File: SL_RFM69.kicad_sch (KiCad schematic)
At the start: 8 parts, among them SW1 SW_DIP_x08

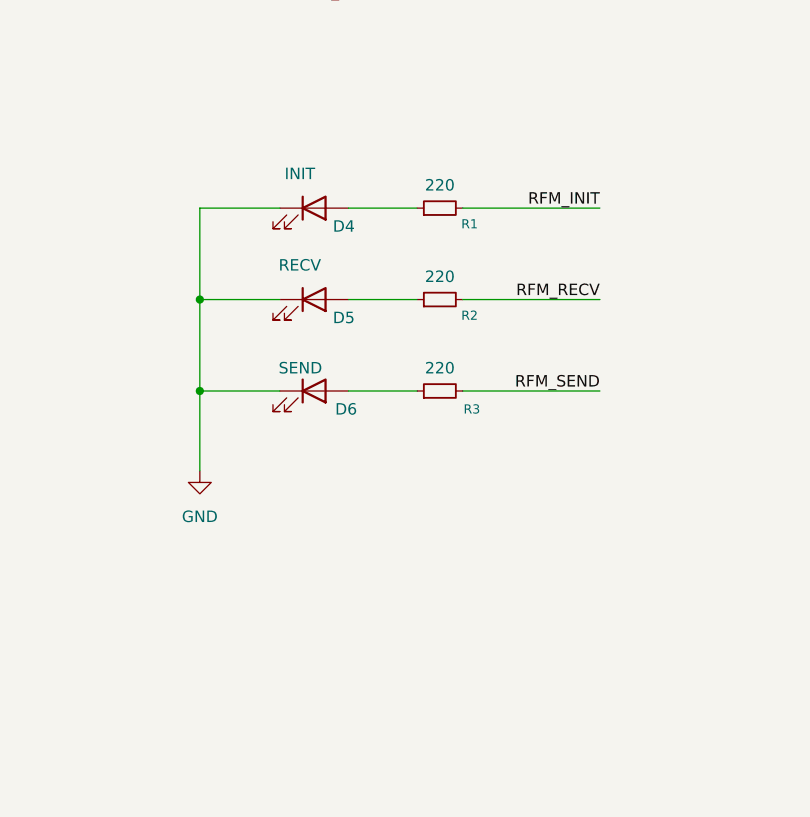
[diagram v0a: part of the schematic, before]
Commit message: Add power led
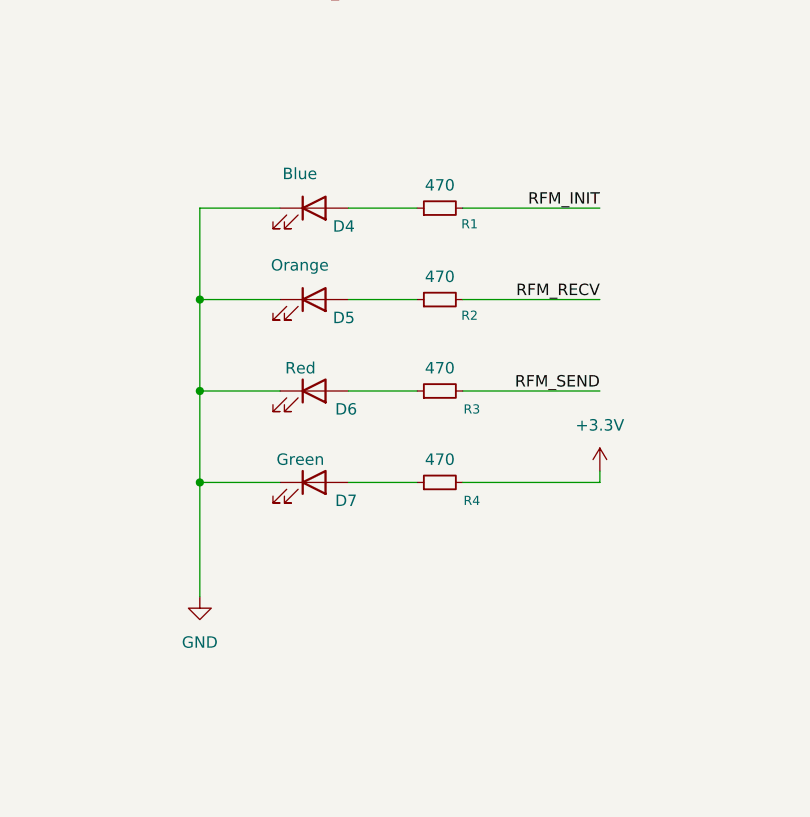
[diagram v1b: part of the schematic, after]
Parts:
- added D7: Green, LED_SMD:LED_0805_2012Metric, symbol Device:LED
- added R4: 470, LED_SMD:LED_0805_2012Metric, symbol Device:R_Small
- D4: value INIT -> Blue
- D5: value RECV -> Orange
- D6: value SEND -> Red
- R1, R2, R3: value 220 -> 470
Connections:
- net +3.3V: now also R4.2
- net GND: now also D7.1 (K)
- new net: D7.2 (A), R4.1

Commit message: Add partnumbers
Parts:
- D4: JLCPCB (none) -> C2293; LCSC (none) -> C2293
- D5: JLCPCB (none) -> C84262; LCSC (none) -> C84262
- D6: JLCPCB (none) -> C84256; LCSC (none) -> C84256
- D7: JLCPCB (none) -> C2297; LCSC (none) -> C2297
- R1, R2, R3, R4: JLCPCB (none) -> C17710; LCSC (none) -> C17710
- SW1: JLCPCB (none) -> C559170
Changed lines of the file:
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@@
+			)
+		)
+		(property "JLCPCB" "C84262"
+			(at 50.8 92.71 0)
+			(hide yes)
+			(show_name no)
+			(do_not_autoplace no)
+			(effects
+				(font
+					(size 1.27 1.27)
+				)
+			)
+		)
+		(property "LCSC" "C84262"
+			(at 50.8 92.71 0)
+			(hide yes)
+			(show_name no)
+			(do_not_autoplace no)
+			(effects
+				(font
+					(size 1.27 1.27)
+				)
 			)
 		)
@@
 		(property "Description" "Resistor, small symbol"
 			(at 64.77 113.03 0)
+			(hide yes)
+			(show_name no)
+			(do_not_autoplace no)
+			(effects
+				(font
+					(size 1.27 1.27)
+				)
+			)
+		)
+		(property "JLCPCB" "C17710"
+			(at 64.77 113.03 90)
+			(hide yes)
+			(show_name no)
+			(do_not_autoplace no)
+			(effects
+				(font
+					(size 1.27 1.27)
+				)
+			)
+		)
+		(property "LCSC" "C17710"
+			(at 64.77 113.03 90)
 			(hide yes)
 			(show_name no)
@@
 			)
 		)
+		(property "JLCPCB" "C2293"
+			(at 50.8 82.55 0)
+			(hide yes)
+			(show_name no)
+			(do_not_autoplace no)
+			(effects
+				(font
+					(size 1.27 1.27)
+				)
+			)
+		)
+		(property "LCSC" "C2293"
+			(at 50.8 82.55 0)
+			(hide yes)
+			(show_name no)
+			(do_not_autoplace no)
+			(effects
+				(font
+					(size 1.27 1.27)
+				)
+			)
+		)
 		(pin "2"
 		)
@@
 			)
 		)
+		(property "JLCPCB" "C84256"
+			(at 50.8 102.87 0)
+			(hide yes)
+			(show_name no)
+			(do_not_autoplace no)
+			(effects
+				(font
+					(size 1.27 1.27)
+				)
+			)
+		)
+		(property "LCSC" "C84256"
+			(at 50.8 102.87 0)
+			(hide yes)
+			(show_name no)
+			(do_not_autoplace no)
+			(effects
+				(font
+					(size 1.27 1.27)
+				)
+			)
+		)
 		(pin "2"
 		)
@@
 		(property "Description" "Resistor, small symbol"
 			(at 64.77 102.87 0)
+			(hide yes)
+			(show_name no)
+			(do_not_autoplace no)
+			(effects
+				(font
+					(size 1.27 1.27)
+				)
+			)
+		)
+		(property "JLCPCB" "C17710"
+			(at 64.77 102.87 90)
+			(hide yes)
+			(show_name no)
+			(do_not_autoplace no)
+			(effects
+				(font
+					(size 1.27 1.27)
+				)
+			)
+		)
+		(property "LCSC" "C17710"
+			(at 64.77 102.87 90)
 			(hide yes)
 			(show_name no)
@@
 			)
 		)
+		(property "JLCPCB" "C17710"
+			(at 64.77 92.71 90)
+			(hide yes)
+			(show_name no)
+			(do_not_autoplace no)
+			(effects
+				(font
+					(size 1.27 1.27)
+				)
+			)
+		)
+		(property "LCSC" "C17710"
+			(at 64.77 92.71 90)
+			(hide yes)
+			(show_name no)
+			(do_not_autoplace no)
+			(effects
+				(font
+					(size 1.27 1.27)
+				)
+			)
+		)
 		(pin "2"
 		)
@@
 			)
 		)
+		(property "JLCPCB" "C559170"
+			(at 135.89 38.1 0)
+			(hide yes)
+			(show_name no)
+			(do_not_autoplace no)
+			(effects
+				(font
+					(size 1.27 1.27)
+				)
+			)
+		)
 		(pin "14"
 		)
@@
 			)
 		)
+		(property "JLCPCB" ""
+			(at 222.25 22.86 0)
+			(hide yes)
+			(show_name no)
+			(do_not_autoplace no)
+			(effects
+				(font
+					(size 1.27 1.27)
+				)
+			)
+		)
 		(pin "B45"
 		)
@@
 			)
 		)
+		(property "JLCPCB" "C17710"
+			(at 64.77 82.55 90)
+			(hide yes)
+			(show_name no)
+			(do_not_autoplace no)
+			(effects
+				(font
+					(size 1.27 1.27)
+				)
+			)
+		)
+		(property "LCSC" "C17710"
+			(at 64.77 82.55 90)
+			(hide yes)
+			(show_name no)
+			(do_not_autoplace no)
+			(effects
+				(font
+					(size 1.27 1.27)
+				)
+			)
+		)
 		(pin "2"
 		)
@@
 			(at 50.8 113.03 0)
 			(hide yes)
+			(show_name no)
+			(do_not_autoplace no)
+			(effects
+				(font
+					(size 1.27 1.27)
+				)
+			)
+		)
+		(property "JLCPCB" "C2297"
+			(at 50.8 113.03 0)
+			(hide yes)
+			(show_name no)
+			(do_not_autoplace no)
+			(effects
+				(font
+					(size 1.27 1.27)
+				)
+			)
+		)
+		(property "LCSC" "C2297"
+			(at 50.8 113.03 0)
+			(hide yes)
